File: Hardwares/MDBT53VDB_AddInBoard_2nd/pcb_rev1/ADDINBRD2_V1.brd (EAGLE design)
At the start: 25 x 31 mm, 21 parts, among them CN1 IF_4PIN, CN2 IF_4PIN, CN3 IF_2PIN, CN4 IF_2PIN, Q1 DMP2035UFDF-7, Q2 BC817-40QA, SW1 SKRPACE010, U1 SN74AHC1G00DRLR, U2 REF3325AIRSER, U3 MCP6232T-E/MNY

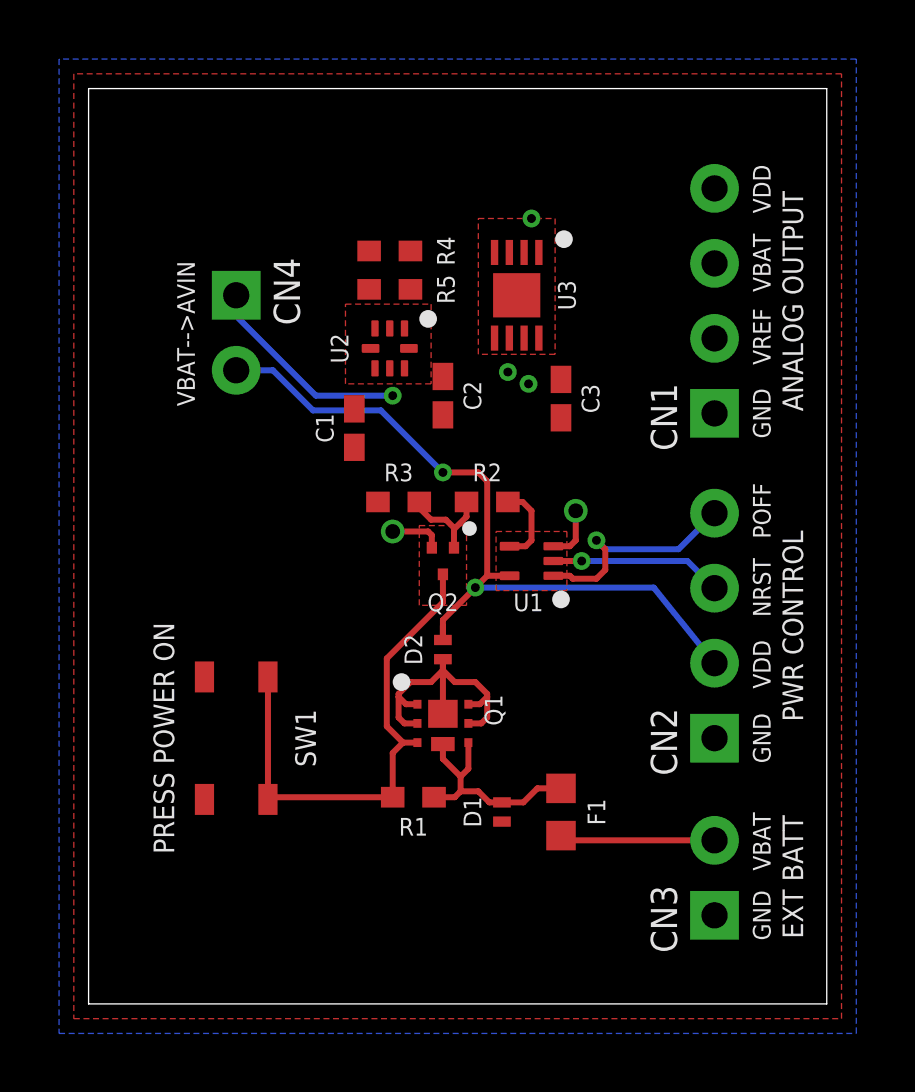
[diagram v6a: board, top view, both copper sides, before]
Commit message: レイアウトを修正
・測定電圧周りを配線
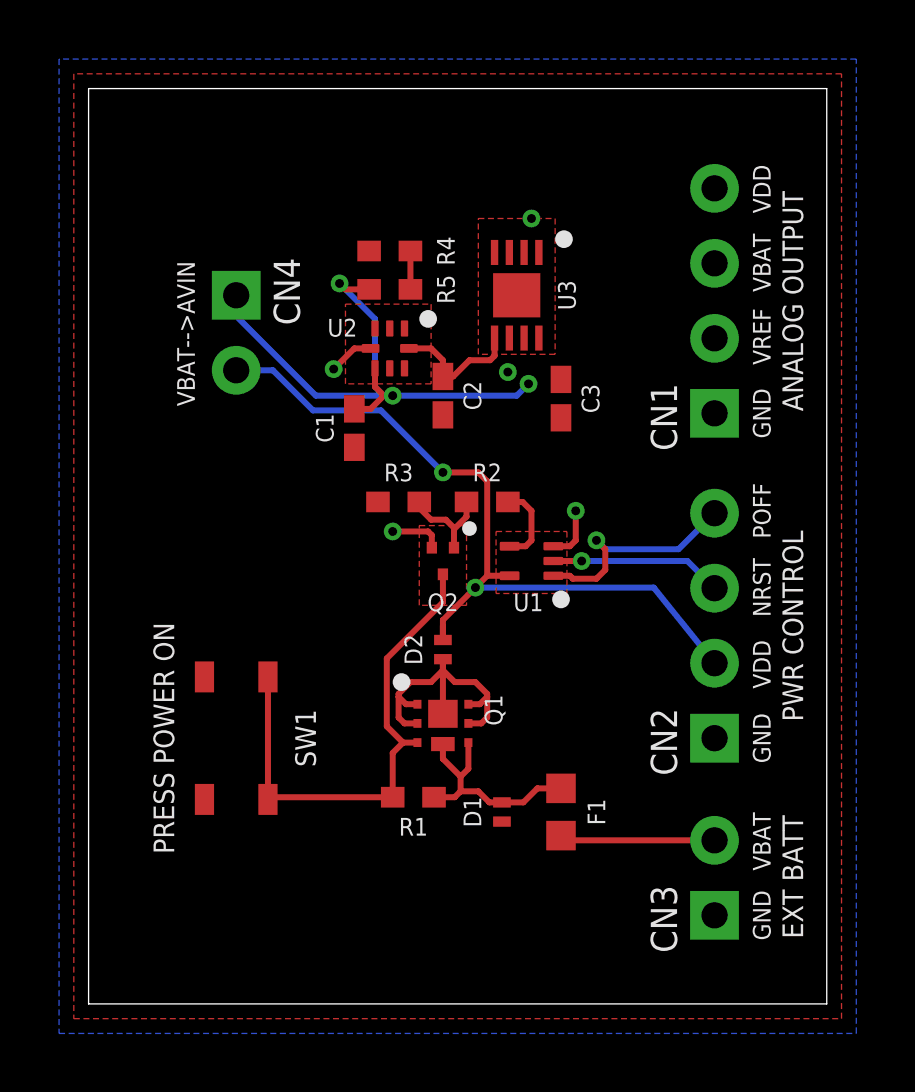
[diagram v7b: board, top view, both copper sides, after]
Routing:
- net AVIN: track 7.12 -> 20.2 mm, vias 2 -> 3
- net AVREF_IN: track 0.00 -> 4.51 mm
- net 0V: track 3.64 -> 5.18 mm, vias 2 -> 3
- net AVBAT_IN: track 0.00 -> 1.30 mm
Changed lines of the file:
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@@
 <element name="U2" library="ICs" package="RSE0008A" value="REF3325AIRSER" x="10.2" y="22.2" smashed="yes" rot="R270">
 <attribute name="VALUE" x="8.2" y="22.6" size="0.6" layer="27" rot="R270"/>
-<attribute name="NAME" x="8.8" y="22.2" size="0.6" layer="25" rot="R90" align="bottom-center"/>
+<attribute name="NAME" x="9.1" y="22.9" size="0.6" layer="25" align="center-right"/>
 </element>
 <element name="C1" library="SMDs" package="C0402" value="1uF" x="9" y="19.5" smashed="yes" rot="R270">
@@
 <contactref element="SW1" pad="1"/>
 <contactref element="SW1" pad="2"/>
-<via x="16.5" y="16.7" extent="1-16" drill="0.5"/>
+<via x="16.5" y="16.7" extent="1-16" drill="0.3"/>
 <contactref element="U2" pad="4"/>
 <contactref element="C1" pad="2"/>
@@
 <wire x1="16.3" y1="15.5" x2="16.5" y2="15.7" width="0.2032" layer="1"/>
 <wire x1="16.5" y1="16.7" x2="16.5" y2="15.7" width="0.2032" layer="1"/>
-<via x="10.3" y="16" extent="1-16" drill="0.5"/>
+<via x="10.3" y="16" extent="1-16" drill="0.3"/>
 <wire x1="11.625" y1="15.45" x2="11.625" y2="15.875" width="0.2032" layer="1"/>
 <wire x1="11.625" y1="15.875" x2="11.5" y2="16" width="0.2032" layer="1"/>
 <wire x1="10.3" y1="16" x2="11.5" y2="16" width="0.2032" layer="1"/>
+<via x="8.3" y="21.5" extent="1-16" drill="0.3"/>
+<wire x1="9.55" y1="22.2" x2="9" y2="22.2" width="0.2032" layer="1"/>
+<wire x1="9" y1="22.2" x2="8.3" y2="21.5" width="0.2032" layer="1"/>
 <wire x1="14.5" y1="24" x2="13.75" y2="25.45" width="0" layer="19" extent="1-1"/>
 <wire x1="9.5" y1="25.5" x2="13.75" y2="25.45" width="0" layer="19" extent="1-1"/>
-<wire x1="9.55" y1="22.2" x2="9.5" y2="25.5" width="0" layer="19" extent="1-1"/>
 </signal>
 <signal name="N$1">
@@
 <contactref element="C2" pad="1"/>
 <contactref element="U3" pad="5"/>
-<wire x1="12" y1="21.25" x2="13.75" y2="22.55" width="0" layer="19" extent="1-1"/>
-<wire x1="10.85" y1="22.2" x2="12" y2="21.25" width="0" layer="19" extent="1-1"/>
+<wire x1="10.85" y1="22.2" x2="11.6" y2="22.2" width="0.2032" layer="1"/>
+<wire x1="12" y1="21.25" x2="12" y2="21.8" width="0.2032" layer="1"/>
+<wire x1="12" y1="21.8" x2="11.6" y2="22.2" width="0.2032" layer="1"/>
+<wire x1="13.75" y1="22.55" x2="13.75" y2="21.95" width="0.2032" layer="1"/>
+<wire x1="13.75" y1="21.95" x2="13.6" y2="21.8" width="0.2032" layer="1"/>
+<wire x1="13.6" y1="21.8" x2="12.9" y2="21.8" width="0.2032" layer="1"/>
+<wire x1="12.9" y1="21.8" x2="12.35" y2="21.25" width="0.2032" layer="1"/>
+<wire x1="12" y1="21.25" x2="12.35" y2="21.25" width="0.2032" layer="1"/>
 </signal>
 <signal name="AVBAT_IN">
@@
 <contactref element="R5" pad="1"/>
 <contactref element="U3" pad="3"/>
+<wire x1="10.9" y1="24.2" x2="10.9" y2="25.5" width="0.2032" layer="1"/>
 <wire x1="10.9" y1="25.5" x2="14.25" y2="25.45" width="0" layer="19" extent="1-1"/>
-<wire x1="10.9" y1="24.2" x2="10.9" y2="25.5" width="0" layer="19" extent="1-1"/>
 </signal>
 <signal name="N$2">
@@
 <via x="10.3" y="20.6" extent="1-16" drill="0.3"/>
 <wire x1="5" y1="24" x2="5" y2="23.3" width="0.2032" layer="16"/>
+<wire x1="5" y1="23.3" x2="7.7" y2="20.6" width="0.2032" layer="16"/>
+<wire x1="10" y1="20.6" x2="9.7" y2="20.9" width="0.2032" layer="1"/>
+<wire x1="9.7" y1="21.525" x2="9.7" y2="20.9" width="0.2032" layer="1"/>
+<wire x1="10.3" y1="20.6" x2="10" y2="20.6" width="0.2032" layer="1"/>
+<wire x1="10" y1="20.6" x2="9.55" y2="20.15" width="0.2032" layer="1"/>
+<wire x1="9" y1="20.15" x2="9.55" y2="20.15" width="0.2032" layer="1"/>
+<wire x1="9.5" y1="24.2" x2="8.7" y2="24.2" width="0.2032" layer="1"/>
+<wire x1="8.7" y1="24.2" x2="8.5" y2="24.4" width="0.2032" layer="1"/>
+<via x="8.5" y="24.4" extent="1-16" drill="0.3"/>
+<wire x1="8.5" y1="24.4" x2="9.7" y2="23.2" width="0.2032" layer="16"/>
+<wire x1="9.7" y1="23.2" x2="9.7" y2="20.9" width="0.2032" layer="16"/>
+<wire x1="9.7" y1="20.9" x2="10" y2="20.6" width="0.2032" layer="16"/>
+<wire x1="10" y1="20.6" x2="10.3" y2="20.6" width="0.2032" layer="16"/>
 <wire x1="7.7" y1="20.6" x2="10.3" y2="20.6" width="0.2032" layer="16"/>
-<wire x1="5" y1="23.3" x2="7.7" y2="20.6" width="0.2032" layer="16"/>
+<wire x1="10.3" y1="20.6" x2="14.5" y2="20.6" width="0.2032" layer="16"/>
+<wire x1="14.9" y1="21" x2="14.5" y2="20.6" width="0.2032" layer="16"/>
 <wire x1="15.25" y1="22.55" x2="21.2" y2="27.62" width="0" layer="19" extent="1-1"/>
 <wire x1="16" y1="21.15" x2="15.25" y2="22.55" width="0" layer="19" extent="1-1"/>
 <wire x1="14.9" y1="21" x2="16" y2="21.15" width="0" layer="19" extent="1-1"/>
-<wire x1="10.3" y1="20.6" x2="14.9" y2="21" width="0" layer="19" extent="1-1"/>
-<wire x1="9.7" y1="21.525" x2="10.3" y2="20.6" width="0" layer="19" extent="1-1"/>
-<wire x1="9" y1="20.15" x2="10.3" y2="20.6" width="0" layer="19" extent="1-1"/>
-<wire x1="9.5" y1="24.2" x2="9.7" y2="21.525" width="0" layer="19" extent="1-1"/>
 </signal>
 <signal name="N$4">
@@
 <vertex x="13.8" y="16"/>
 <vertex x="16.2" y="16"/>
-<vertex x="16.2" y="14"/>
-<vertex x="13.8" y="14"/>
+<vertex x="16.2" y="13.9"/>
+<vertex x="13.8" y="13.9"/>
 </polygon>
 <polygon width="0" layer="1" pour="cutout" isolate="0.2032">

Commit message: レイアウトを修正
・バッファ周りを配線
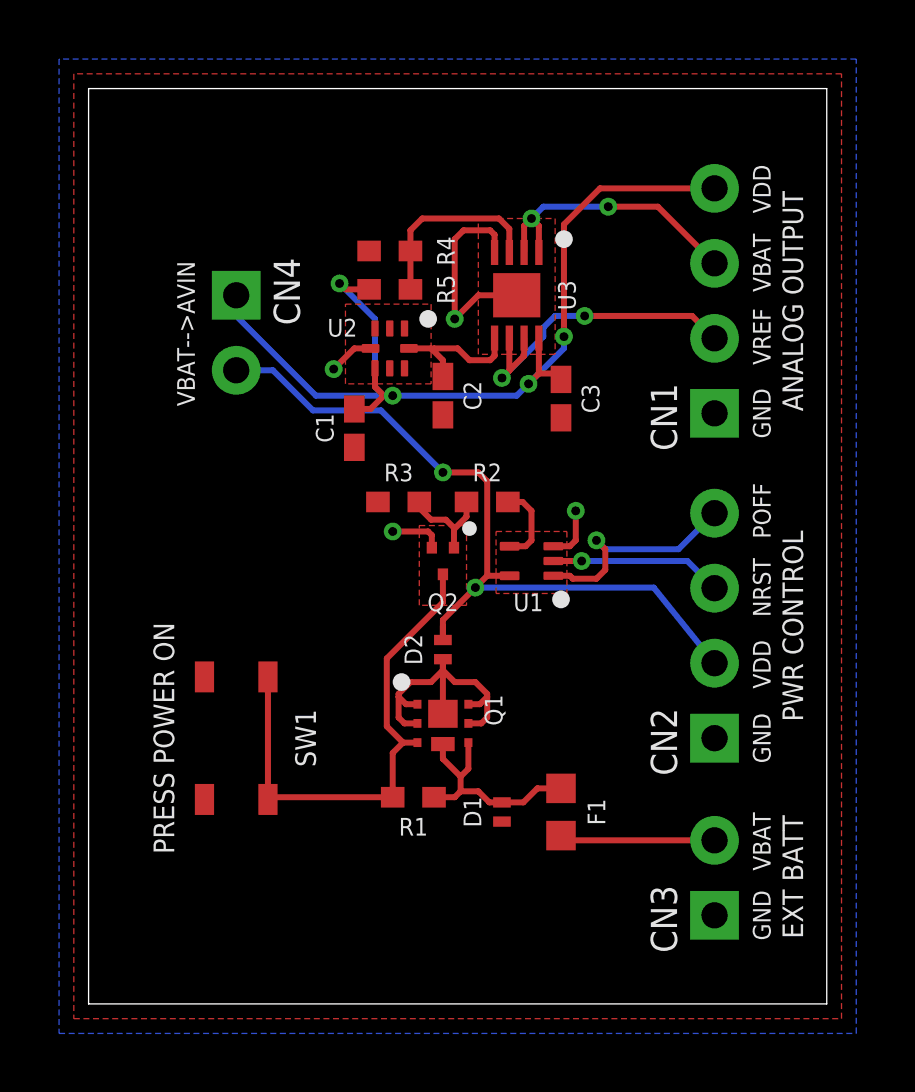
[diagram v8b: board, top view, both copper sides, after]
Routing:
- net AVIN: track 20.2 -> 34.3 mm, vias 3 -> 4
- net AVREF: track 0.00 -> 11.7 mm, vias 1 -> 2
- net AVBAT: track 0.00 -> 9.67 mm, vias 1 -> 2
- net 0V: track 5.18 -> 12.5 mm, vias 3 -> 4
- net AVBAT_IN: track 1.30 -> 6.46 mm
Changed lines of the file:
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@@
 <wire x1="9.55" y1="22.2" x2="9" y2="22.2" width="0.2032" layer="1"/>
 <wire x1="9" y1="22.2" x2="8.3" y2="21.5" width="0.2032" layer="1"/>
-<wire x1="14.5" y1="24" x2="13.75" y2="25.45" width="0" layer="19" extent="1-1"/>
-<wire x1="9.5" y1="25.5" x2="13.75" y2="25.45" width="0" layer="19" extent="1-1"/>
+<via x="12.4" y="23.2" extent="1-16" drill="0.3"/>
+<wire x1="14.5" y1="24" x2="13.2" y2="24" width="0.2032" layer="1"/>
+<wire x1="13.2" y1="24" x2="12.4" y2="23.2" width="0.2032" layer="1"/>
+<wire x1="13.75" y1="25.45" x2="13.75" y2="26.05" width="0.2032" layer="1"/>
+<wire x1="13.75" y1="26.05" x2="13.6" y2="26.2" width="0.2032" layer="1"/>
+<wire x1="13.6" y1="26.2" x2="12.7" y2="26.2" width="0.2032" layer="1"/>
+<wire x1="12.7" y1="26.2" x2="12.4" y2="25.9" width="0.2032" layer="1"/>
+<wire x1="12.4" y1="25.9" x2="12.4" y2="23.2" width="0.2032" layer="1"/>
 </signal>
 <signal name="N$1">
@@
 <wire x1="10.85" y1="22.2" x2="11.6" y2="22.2" width="0.2032" layer="1"/>
 <wire x1="12" y1="21.25" x2="12" y2="21.8" width="0.2032" layer="1"/>
-<wire x1="12" y1="21.8" x2="11.6" y2="22.2" width="0.2032" layer="1"/>
+<wire x1="12" y1="21.8" x2="11.65" y2="22.15" width="0.2032" layer="1"/>
+<wire x1="11.65" y1="22.15" x2="11.6" y2="22.2" width="0.2032" layer="1"/>
 <wire x1="13.75" y1="22.55" x2="13.75" y2="21.95" width="0.2032" layer="1"/>
 <wire x1="13.75" y1="21.95" x2="13.6" y2="21.8" width="0.2032" layer="1"/>
 <wire x1="13.6" y1="21.8" x2="12.9" y2="21.8" width="0.2032" layer="1"/>
-<wire x1="12.9" y1="21.8" x2="12.35" y2="21.25" width="0.2032" layer="1"/>
-<wire x1="12" y1="21.25" x2="12.35" y2="21.25" width="0.2032" layer="1"/>
+<wire x1="12.9" y1="21.8" x2="12.5" y2="22.2" width="0.2032" layer="1"/>
+<wire x1="12.5" y1="22.2" x2="11.7" y2="22.2" width="0.2032" layer="1"/>
+<wire x1="11.7" y1="22.2" x2="11.65" y2="22.15" width="0.2032" layer="1"/>
 </signal>
 <signal name="AVBAT_IN">
@@
 <contactref element="U3" pad="3"/>
 <wire x1="10.9" y1="24.2" x2="10.9" y2="25.5" width="0.2032" layer="1"/>
-<wire x1="10.9" y1="25.5" x2="14.25" y2="25.45" width="0" layer="19" extent="1-1"/>
+<wire x1="10.9" y1="25.5" x2="10.9" y2="26.2" width="0.2032" layer="1"/>
+<wire x1="14.25" y1="25.45" x2="14.25" y2="26.25" width="0.2032" layer="1"/>
+<wire x1="10.9" y1="26.2" x2="11.3" y2="26.6" width="0.2032" layer="1"/>
+<wire x1="11.3" y1="26.6" x2="13.9" y2="26.6" width="0.2032" layer="1"/>
+<wire x1="14.25" y1="26.25" x2="13.9" y2="26.6" width="0.2032" layer="1"/>
 </signal>
 <signal name="N$2">
@@
 <contactref element="CN1" pad="3"/>
 <via x="15" y="26.6" extent="1-16" drill="0.3"/>
-<wire x1="15.25" y1="25.45" x2="21.2" y2="25.08" width="0" layer="19" extent="1-1"/>
-<wire x1="14.75" y1="25.45" x2="15.25" y2="25.45" width="0" layer="19" extent="1-1"/>
-<wire x1="15" y1="26.6" x2="15.25" y2="25.45" width="0" layer="19" extent="1-1"/>
+<wire x1="15.25" y1="25.45" x2="15.25" y2="26.35" width="0.2032" layer="1"/>
+<wire x1="15.25" y1="26.35" x2="15" y2="26.6" width="0.2032" layer="1"/>
+<wire x1="14.75" y1="25.45" x2="14.75" y2="26.35" width="0.2032" layer="1"/>
+<wire x1="14.75" y1="26.35" x2="15" y2="26.6" width="0.2032" layer="1"/>
+<via x="17.6" y="27" extent="1-16" drill="0.3"/>
+<wire x1="21.2" y1="25.08" x2="19.28" y2="27" width="0.2032" layer="1"/>
+<wire x1="19.28" y1="27" x2="17.6" y2="27" width="0.2032" layer="1"/>
+<wire x1="17.6" y1="27" x2="15.4" y2="27" width="0.2032" layer="16"/>
+<wire x1="15.4" y1="27" x2="15" y2="26.6" width="0.2032" layer="16"/>
 </signal>
 <signal name="AVREF">
@@
 <contactref element="U3" pad="6"/>
 <contactref element="CN1" pad="2"/>
-<via x="14.2" y="21.4" extent="1-16" drill="0.3"/>
-<wire x1="14.75" y1="22.55" x2="21.2" y2="22.54" width="0" layer="19" extent="1-1"/>
-<wire x1="14.25" y1="22.55" x2="14.75" y2="22.55" width="0" layer="19" extent="1-1"/>
-<wire x1="14.2" y1="21.4" x2="14.25" y2="22.55" width="0" layer="19" extent="1-1"/>
+<via x="14" y="21.2" extent="1-16" drill="0.3"/>
+<wire x1="14.25" y1="22.55" x2="14.25" y2="21.45" width="0.2032" layer="1"/>
+<wire x1="14.25" y1="21.45" x2="14" y2="21.2" width="0.2032" layer="1"/>
+<wire x1="14" y1="21.2" x2="15.4" y2="22.6" width="0.2032" layer="16"/>
+<wire x1="15.4" y1="22.6" x2="15.4" y2="22.9" width="0.2032" layer="16"/>
+<wire x1="15.4" y1="22.9" x2="15.8" y2="23.3" width="0.2032" layer="16"/>
+<wire x1="14.75" y1="22.55" x2="14.75" y2="21.95" width="0.2032" layer="1"/>
+<wire x1="14.75" y1="21.95" x2="14" y2="21.2" width="0.2032" layer="1"/>
+<via x="16.8" y="23.3" extent="1-16" drill="0.3"/>
+<wire x1="15.8" y1="23.3" x2="16.8" y2="23.3" width="0.2032" layer="16"/>
+<wire x1="21.2" y1="22.54" x2="20.44" y2="23.3" width="0.2032" layer="1"/>
+<wire x1="20.44" y1="23.3" x2="16.8" y2="23.3" width="0.2032" layer="1"/>
 </signal>
 <signal name="AVIN">
@@
 <wire x1="10.3" y1="20.6" x2="14.5" y2="20.6" width="0.2032" layer="16"/>
 <wire x1="14.9" y1="21" x2="14.5" y2="20.6" width="0.2032" layer="16"/>
-<wire x1="15.25" y1="22.55" x2="21.2" y2="27.62" width="0" layer="19" extent="1-1"/>
-<wire x1="16" y1="21.15" x2="15.25" y2="22.55" width="0" layer="19" extent="1-1"/>
-<wire x1="14.9" y1="21" x2="16" y2="21.15" width="0" layer="19" extent="1-1"/>
+<wire x1="15.25" y1="22.55" x2="15.25" y2="21.35" width="0.2032" layer="1"/>
+<wire x1="15.25" y1="21.35" x2="14.9" y2="21" width="0.2032" layer="1"/>
+<wire x1="15.25" y1="21.35" x2="15.8" y2="21.35" width="0.2032" layer="1"/>
+<wire x1="15.8" y1="21.35" x2="16" y2="21.15" width="0.2032" layer="1"/>
+<via x="16.1" y="22.6" extent="1-16" drill="0.3"/>
+<wire x1="16.1" y1="22.2" x2="14.9" y2="21" width="0.2032" layer="16"/>
+<wire x1="16.1" y1="22.2" x2="16.1" y2="22.6" width="0.2032" layer="16"/>
+<wire x1="21.2" y1="27.62" x2="17.32" y2="27.62" width="0.2032" layer="1"/>
+<wire x1="17.32" y1="27.62" x2="16.1" y2="26.4" width="0.2032" layer="1"/>
+<wire x1="16.1" y1="26.4" x2="16.1" y2="22.6" width="0.2032" layer="1"/>
 </signal>
 <signal name="N$4">
